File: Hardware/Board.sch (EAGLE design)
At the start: 49 parts, among them J1 OUT, J2 POWER, J3 ICSP, SW1 ROTARTY_ENCODER, U1 ATTINY2313A, U2 AW9523B

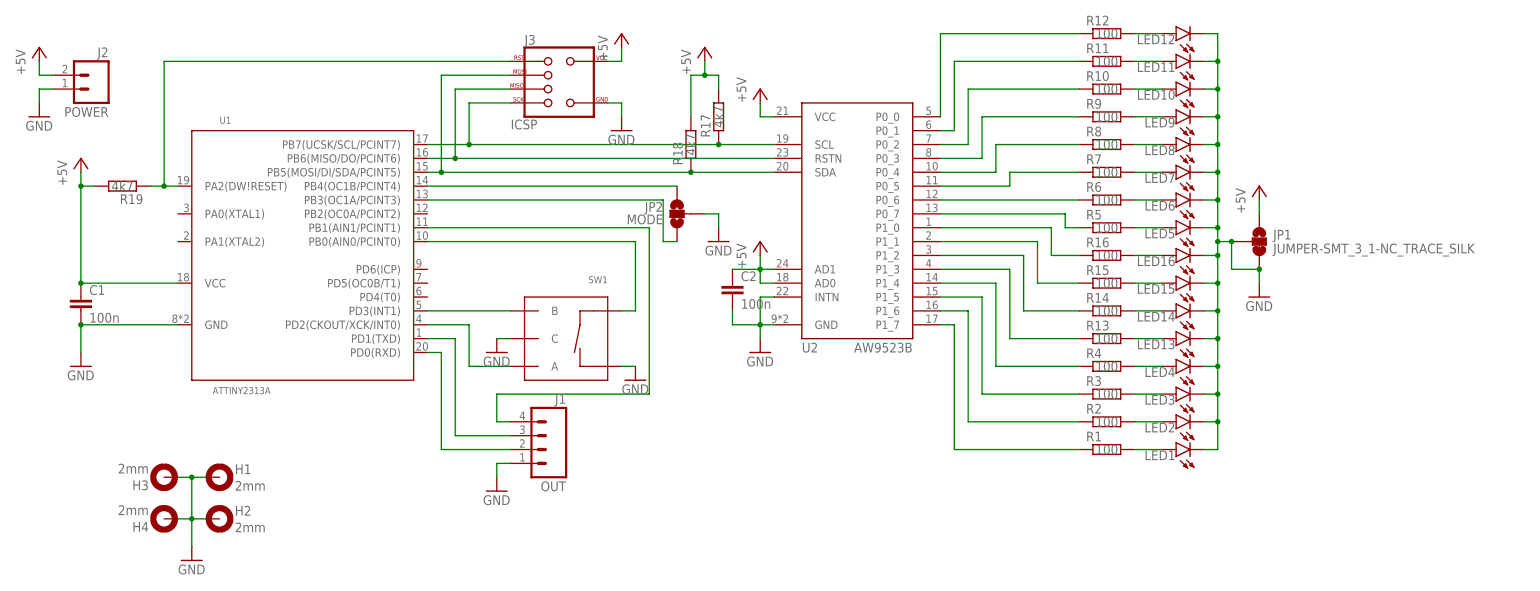
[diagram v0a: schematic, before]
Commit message: updated board layout to optimize for DFM
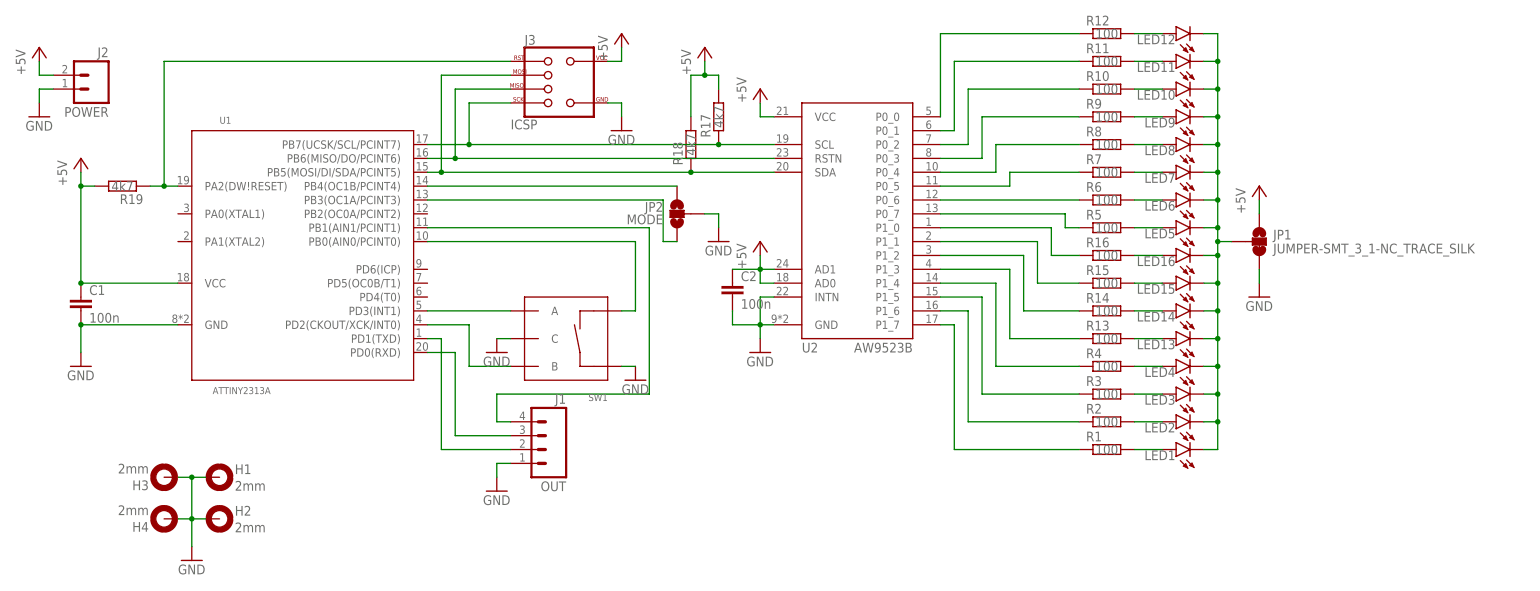
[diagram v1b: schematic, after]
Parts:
- J3: device MiniISP:MINI-ISP-LOCK -> MiniISP:MINI-ISP-LABELS
- U1: LCSC (none) -> C185530
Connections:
- removed net VCC: C1.1, R19.2, U1.VCC
- new net N$45: JP1.2, LED1.C, LED10.C, LED11.C, LED12.C, LED13.C, LED14.C, LED15.C, LED16.C, LED2.C, LED3.C, LED4.C, LED5.C, LED6.C, LED7.C, LED8.C, LED9.C
- net +5V: now also C1.1, R19.2, U1.VCC
- net GND: now also SW1.SW+; no longer JP1.2, LED1.C, LED10.C, LED11.C, LED12.C, LED13.C, LED14.C, LED15.C, LED16.C, LED2.C, LED3.C, LED4.C, LED5.C, LED6.C, LED7.C, LED8.C, LED9.C, SW1.SW-
- net N$20: now also J1.3; no longer J1.2
- net N$37: now also SW1.A; no longer SW1.B
- net N$38: now also SW1.SW-; no longer SW1.SW+
- net N$39: now also J1.2; no longer J1.3
- net N$40: now also SW1.B; no longer SW1.A
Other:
- moved on the sheet: SW1
